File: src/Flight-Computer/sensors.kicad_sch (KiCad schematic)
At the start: 36 parts, among them P5 440054-3, P6 440054-3, P7 440054-3, P9 440054-3, Q3 QS5U17TR, Q4 QS5U17TR, Q5 QS5U17TR, Q6 QS5U17TR, U11 BMP390, U8 MPU-9250, U9 MAX-8C-0-10

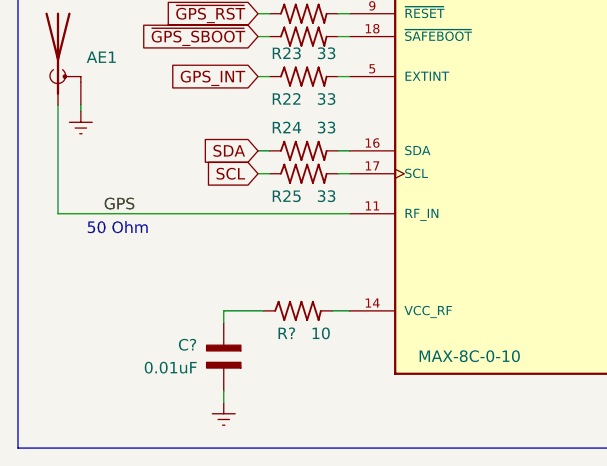
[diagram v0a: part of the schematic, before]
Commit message: added power supply for active gps antenna
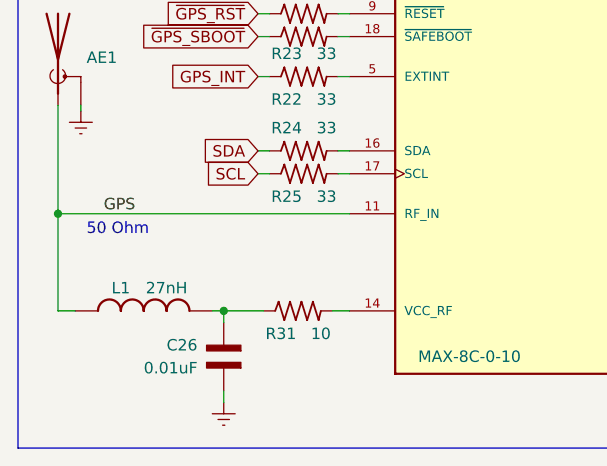
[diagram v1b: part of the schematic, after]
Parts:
- added L1: 27nH, symbol Flight-Computer:L-07C27NJV6T
- gave numbers to parts that had none: 2
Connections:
- net GPS: now also L1.1
- net at C26.1, R31.1: now also L1.2
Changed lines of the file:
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@@
   (junction (at 175.895 124.46) (diameter 0) (color 0 0 0 0)
   )
+  (junction (at 22.86 121.285) (diameter 0) (color 0 0 0 0)
+  )
   (junction (at 97.155 68.58) (diameter 0) (color 0 0 0 0)
   )
@@
   )
   (junction (at 97.155 38.1) (diameter 0) (color 0 0 0 0)
+  )
+  (junction (at 41.275 132.08) (diameter 0) (color 0 0 0 0)
   )
   (junction (at 232.41 40.005) (diameter 0) (color 0 0 0 0)
@@
     (stroke (width 0) (type default) (color 0 0 0 0))
   )
+  (wire (pts (xy 22.86 121.285) (xy 55.245 121.285))
+    (stroke (width 0) (type default) (color 0 0 0 0))
+  )
   (wire (pts (xy 100.965 123.825) (xy 102.235 123.825))
     (stroke (width 0) (type default) (color 0 0 0 0))
@@
     (stroke (width 0) (type default) (color 0 0 0 0))
   )
-  (wire (pts (xy 55.245 121.285) (xy 22.86 121.285))
-    (stroke (width 0) (type default) (color 0 0 0 0))
-  )
   (wire (pts (xy 97.155 53.34) (xy 97.155 38.1))
     (stroke (width 0) (type default) (color 0 0 0 0))
@@
     (stroke (width 0) (type default) (color 0 0 0 0))
   )
+  (wire (pts (xy 22.86 132.08) (xy 24.765 132.08))
+    (stroke (width 0) (type default) (color 0 0 0 0))
+  )
   (wire (pts (xy 232.41 95.885) (xy 232.41 105.41))
     (stroke (width 0) (type default) (color 0 0 0 0))
@@
     (stroke (width 0) (type default) (color 0 0 0 0))
   )
+  (wire (pts (xy 40.005 132.08) (xy 41.275 132.08))
+    (stroke (width 0) (type default) (color 0 0 0 0))
+  )
   (wire (pts (xy 121.285 35.56) (xy 121.285 36.83))
     (stroke (width 0) (type default) (color 0 0 0 0))
@@
   )
   (wire (pts (xy 53.34 132.08) (xy 55.245 132.08))
+    (stroke (width 0) (type default) (color 0 0 0 0))
+  )
+  (wire (pts (xy 22.86 121.285) (xy 22.86 132.08))
     (stroke (width 0) (type default) (color 0 0 0 0))
   )
@@
   (symbol (lib_id "Flight-Computer:Earth") (at 41.275 142.24 0) (unit 1)
     (in_bom yes) (on_board yes) (fields_autoplaced)
-    (property "Reference" "#PWR?" (id 0) (at 41.275 148.59 0)
+    (property "Reference" "#PWR057" (id 0) (at 41.275 148.59 0)
       (effects (font (size 1.27 1.27)) hide)
     )
@@
   (symbol (lib_id "Flight-Computer:RES_0603") (at 49.53 132.08 0) (unit 1)
     (in_bom yes) (on_board yes)
-    (property "Reference" "R?" (id 0) (at 48.26 134.62 0))
+    (property "Reference" "R31" (id 0) (at 47.625 134.62 0))
     (property "Value" "10" (id 1) (at 52.07 134.62 0))
     (property "Footprint" "" (id 2) (at 50.8 144.78 0)
@@
     )
     (pin "1")
+  )
+  (symbol (lib_id "Flight-Computer:L-07C27NJV6T") (at 32.385 132.08 0) (unit 1)
+    (in_bom yes) (on_board yes)
+    (property "Reference" "L1" (id 0) (at 29.845 129.54 0))
+    (property "Value" "27nH" (id 1) (at 34.925 129.54 0))
+    (property "Footprint" "" (id 2) (at 28.575 137.16 0)
+      (effects (font (size 1.27 1.27)) (justify left bottom) hide)
+    )
+    (property "Datasheet" "" (id 3) (at 32.385 132.08 0)
+      (effects (font (size 1.27 1.27)) (justify left bottom) hide)
+    )
+    (pin "1")
+    (pin "2")
   )
   (symbol (lib_id "Flight-Computer:RES_0603") (at 50.165 114.3 0) (unit 1)
@@
   (symbol (lib_id "Flight-Computer:CAP_0603") (at 41.275 137.16 90) (unit 1)
     (in_bom yes) (on_board yes)
-    (property "Reference" "C?" (id 0) (at 36.195 135.89 90)
+    (property "Reference" "C26" (id 0) (at 34.925 135.89 90)
       (effects (font (size 1.27 1.27)) (justify right))
     )

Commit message: plotted schematic to pdf
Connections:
- no-connect marks 7 -> 6
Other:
- note removed: "TODO: Add antenna power connections"
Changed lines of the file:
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@@
   (junction (at 52.705 55.88) (diameter 0) (color 0 0 0 0)
   )
-  (no_connect (at 100.965 106.045))
   (no_connect (at 100.965 127.635))
   (no_connect (at 100.965 111.125))
@@
     (stroke (width 0) (type default) (color 0 0 0 0))
   )
-  (text "TODO: Add antenna\npower connections" (at 103.505 109.855 0)
-    (effects (font (size 1.27 1.27)) (justify left bottom))
-  )
   (text "Servo Motor PWM Interface" (at 187.325 86.995 0)

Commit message: added mcu signals for peripherals
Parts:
- AE1: footprint (none) -> Flight-Computer:73412-0110
- BT1: footprint (none) -> Flight-Computer:MS621FE-FL11E
- C20, C21, C22, C24, C25, C26: footprint (none) -> Flight-Computer:CAP_0603
- D10, D7, D8, D9: footprint (none) -> Flight-Computer:MM3Z3V3B
- L1: footprint (none) -> Flight-Computer:L-07C27NJV6T
- P5, P6, P7, P9: footprint CONN_4840.2201_SCH -> Flight-Computer:440054-3
- R19, R20, R21, R22, R23, R24, R25, R26, R27, R28, R29, R30, R31: footprint (none) -> Flight-Computer:RES_0603
- U11: footprint XDCR_BMP390L -> Flight-Computer:BMP390
- U8: footprint QFN40P300X300X105-24N -> Flight-Computer:MPU-9250
- U9: footprint XCVR_MAX-8C-0-10 -> Flight-Computer:MAX-8C-0

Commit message: setup layout design rules
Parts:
- Q3, Q4, Q5, Q6: footprint Package_TO_SOT_THT:TO-92_Inline -> Engine-Controller:QS5U17TR
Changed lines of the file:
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@@
     (pin "1")
   )
-  (symbol (lib_id "Flight-Computer:QS5U17TR") (at 182.88 104.775 0) (unit 1)
+  (symbol (lib_name "QS5U17TR_1") (lib_id "Flight-Computer:QS5U17TR") (at 182.88 104.775 0) (unit 1)
     (in_bom yes) (on_board yes) (fields_autoplaced)
     (property "Reference" "Q3" (id 0) (at 188.087 105.2088 0)
@@
       (effects (font (size 1.27 1.27)) (justify left) hide)
     )
-    (property "Footprint" "Package_TO_SOT_THT:TO-92_Inline" (id 2) (at 184.785 120.65 0)
+    (property "Footprint" "Engine-Controller:QS5U17TR" (id 2) (at 184.785 120.65 0)
       (effects (font (size 1.27 1.27) italic) (justify left) hide)
     )
@@
     (pin "1")
     (pin "2")
+    (pin "3")
+    (pin "4")
     (pin "5")
   )
@@
     (pin "2")
   )
-  (symbol (lib_id "Flight-Computer:QS5U17TR") (at 182.88 132.715 0) (unit 1)
+  (symbol (lib_name "QS5U17TR_2") (lib_id "Flight-Computer:QS5U17TR") (at 182.88 132.715 0) (unit 1)
     (in_bom yes) (on_board yes) (fields_autoplaced)
     (property "Reference" "Q4" (id 0) (at 188.087 133.1488 0)
@@
       (effects (font (size 1.27 1.27)) (justify left) hide)
     )
-    (property "Footprint" "Package_TO_SOT_THT:TO-92_Inline" (id 2) (at 184.785 148.59 0)
+    (property "Footprint" "Engine-Controller:QS5U17TR" (id 2) (at 184.785 148.59 0)
       (effects (font (size 1.27 1.27) italic) (justify left) hide)
     )
@@
     (pin "1")
     (pin "2")
+    (pin "3")
+    (pin "4")
     (pin "5")
   )
@@
       (effects (font (size 1.27 1.27)) (justify left) hide)
     )
-    (property "Footprint" "Package_TO_SOT_THT:TO-92_Inline" (id 2) (at 241.3 120.015 0)
+    (property "Footprint" "Engine-Controller:QS5U17TR" (id 2) (at 241.3 120.015 0)
       (effects (font (size 1.27 1.27) italic) (justify left) hide)
     )
@@
     (pin "1")
     (pin "2")
+    (pin "3")
+    (pin "4")
     (pin "5")
   )
@@
     (pin "1")
   )
-  (symbol (lib_id "Flight-Computer:QS5U17TR") (at 239.395 132.08 0) (unit 1)
+  (symbol (lib_name "QS5U17TR_3") (lib_id "Flight-Computer:QS5U17TR") (at 239.395 132.08 0) (unit 1)
     (in_bom yes) (on_board yes) (fields_autoplaced)
     (property "Reference" "Q6" (id 0) (at 244.602 132.5138 0)
@@
       (effects (font (size 1.27 1.27)) (justify left) hide)
     )
-    (property "Footprint" "Package_TO_SOT_THT:TO-92_Inline" (id 2) (at 241.3 147.955 0)
+    (property "Footprint" "Engine-Controller:QS5U17TR" (id 2) (at 241.3 147.955 0)
       (effects (font (size 1.27 1.27) italic) (justify left) hide)
     )
@@
     (pin "1")
     (pin "2")
+    (pin "3")
+    (pin "4")
     (pin "5")
   )
@@
     (pin "8")
     (pin "9")
+    (pin "14")
+    (pin "15")
+    (pin "16")
+    (pin "17")
+    (pin "2")
+    (pin "3")
+    (pin "4")
+    (pin "5")
+    (pin "6")
   )
   (symbol (lib_id "Flight-Computer:MS614SE-FL28E") (at 125.73 107.315 0) (unit 1)

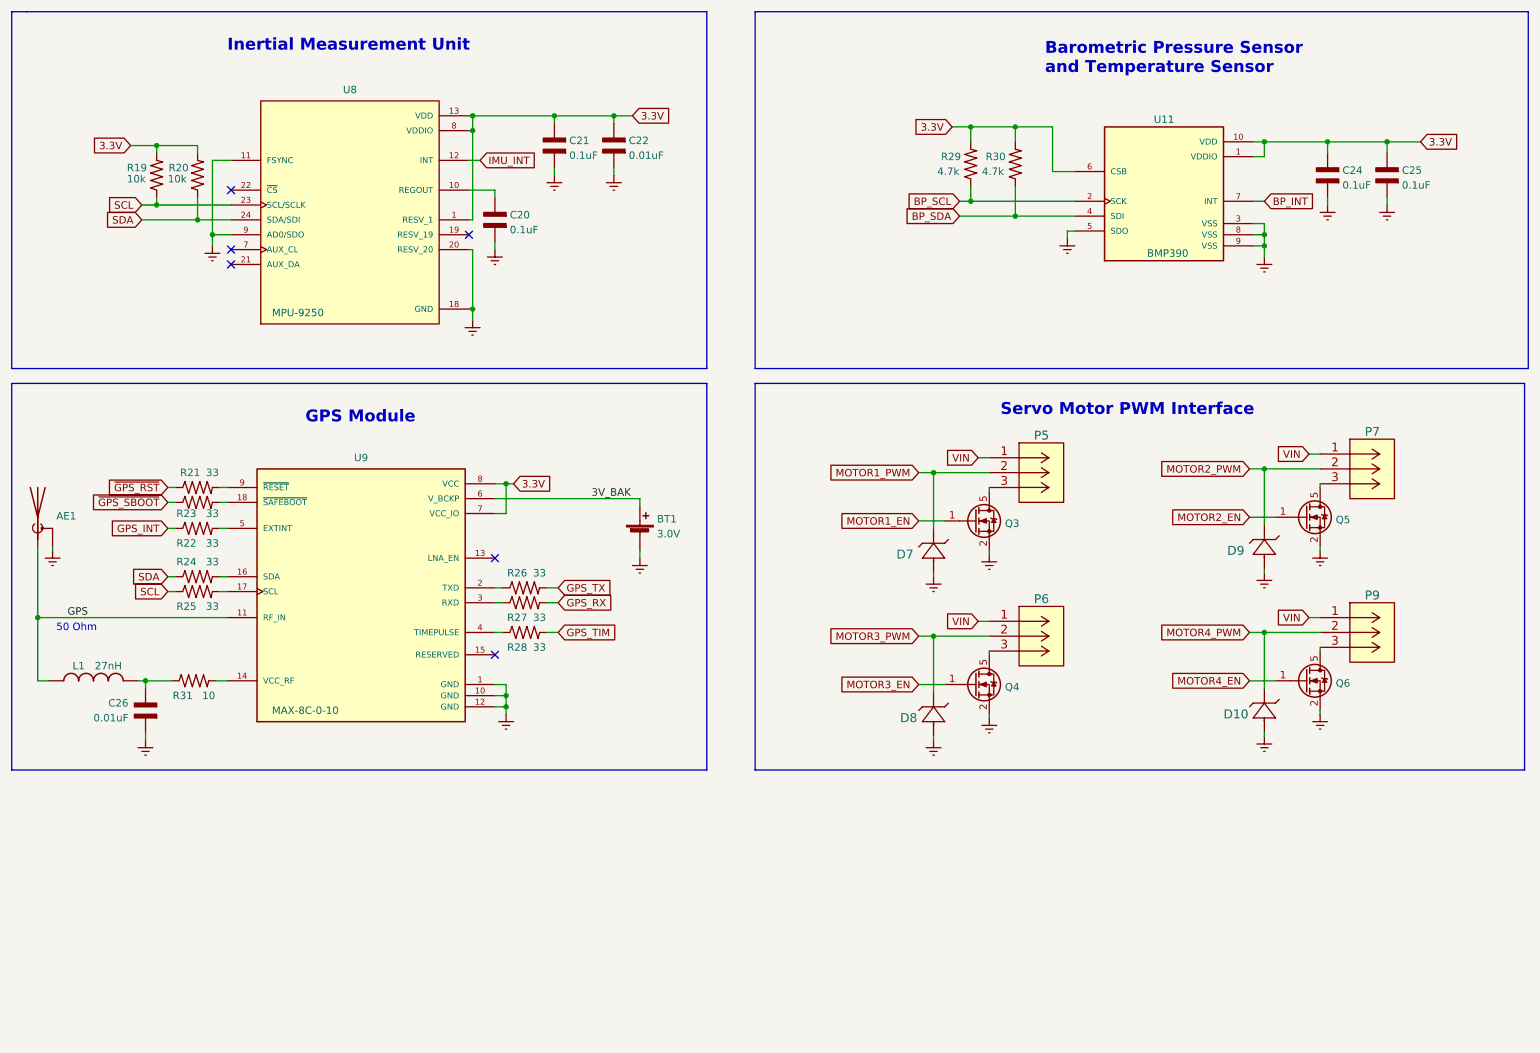
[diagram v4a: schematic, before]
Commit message: added usb detector to schemtaic
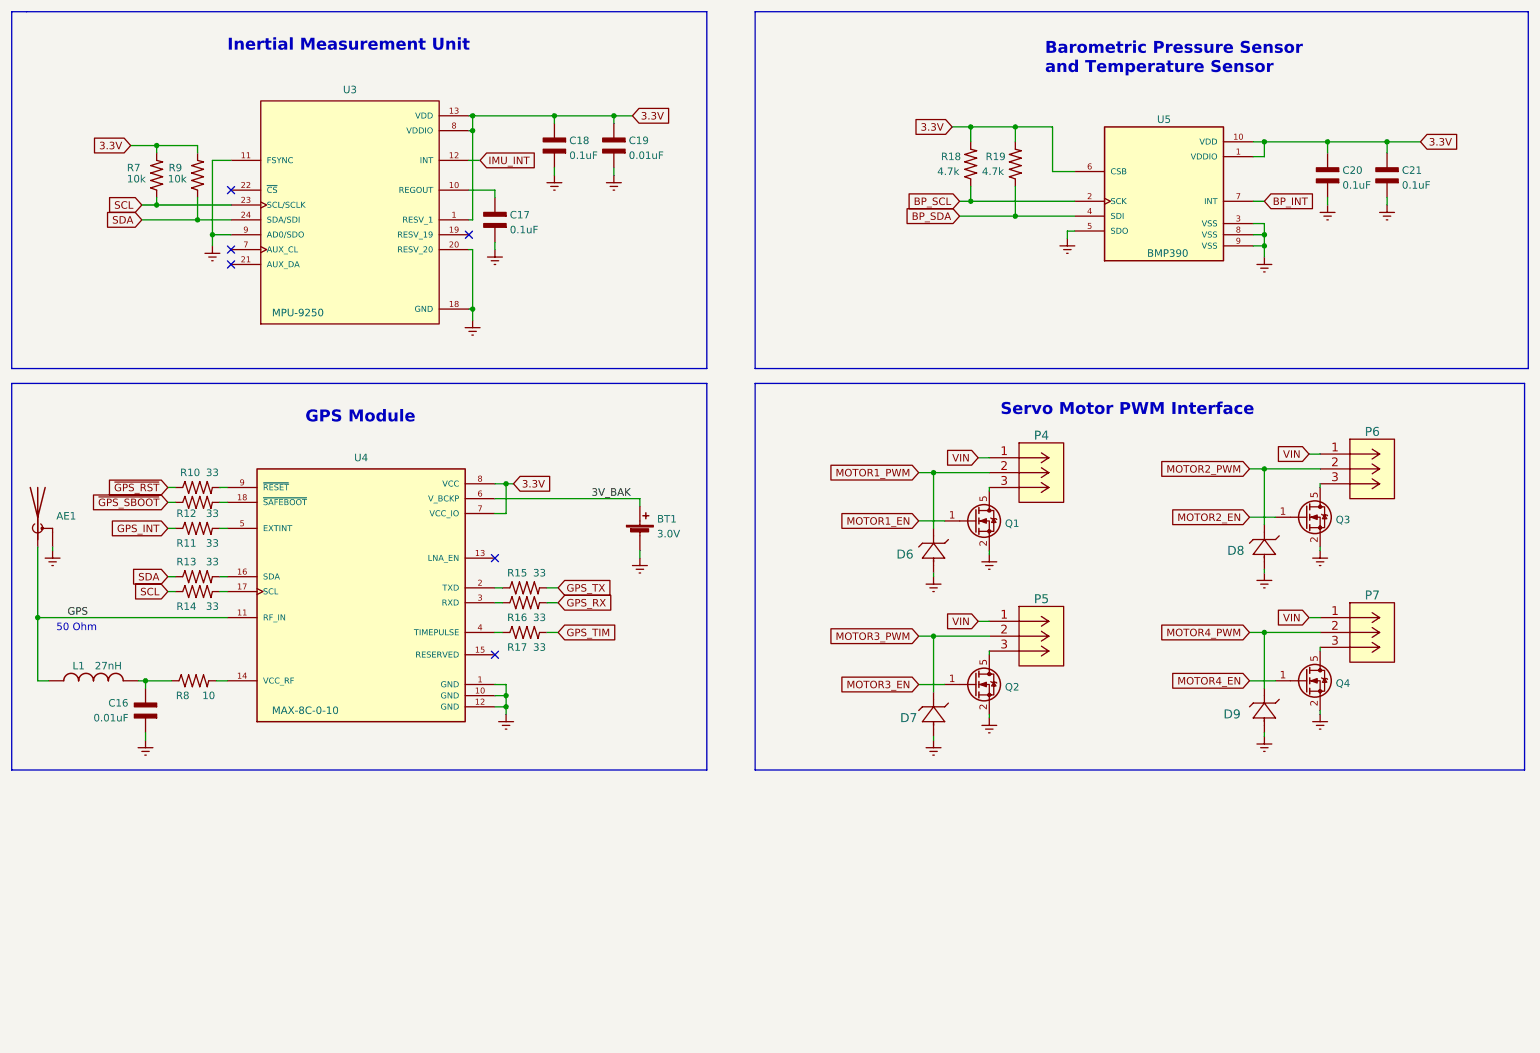
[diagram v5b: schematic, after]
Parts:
- renumbered C26 to C16, C20 to C17, C21 to C18, C22 to C19, C24 to C20, C25 to C21, D7 to D6, D8 to D7, D9 to D8, D10 to D9, P5 to P4, P6 to P5, P7 to P6, P9 to P7, Q3 to Q1, Q4 to Q2, Q5 to Q3, Q6 to Q4, R21 to R10, R22 to R11, R23 to R12, R24 to R13, R25 to R14, R26 to R15, R27 to R16, R28 to R17, R29 to R18, R30 to R19, R19 to R7, R31 to R8, R20 to R9, U8 to U3, U9 to U4, U11 to U5

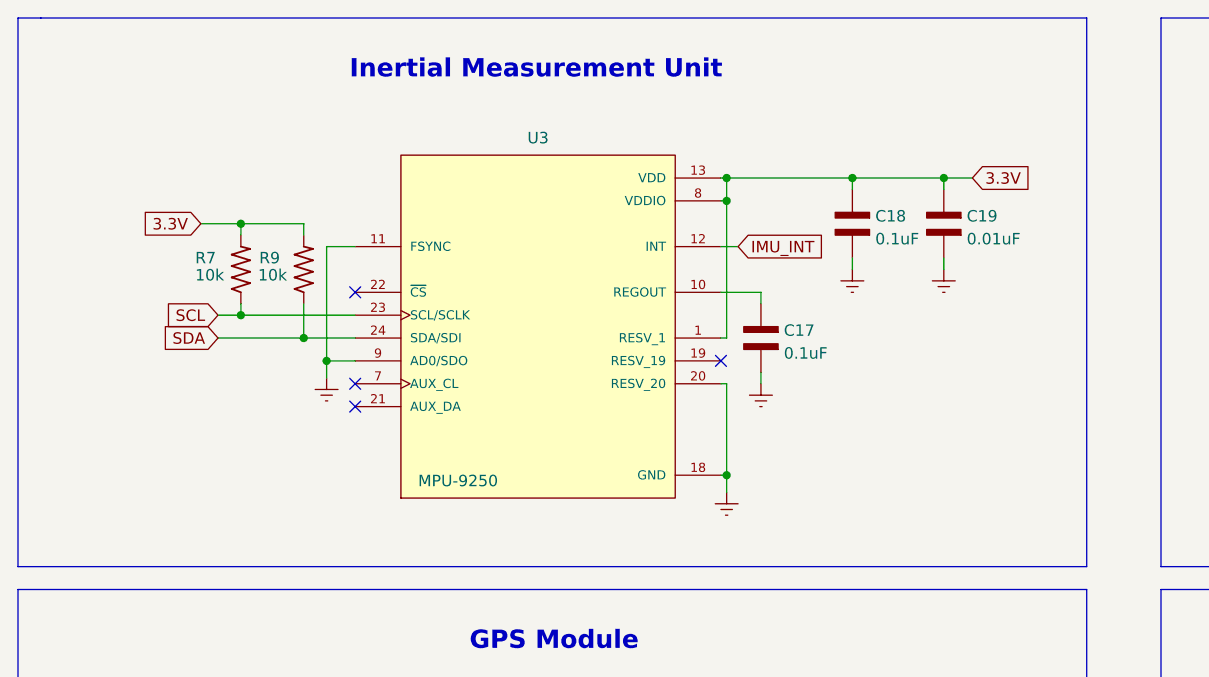
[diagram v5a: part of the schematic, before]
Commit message: implemented new imu in schematic
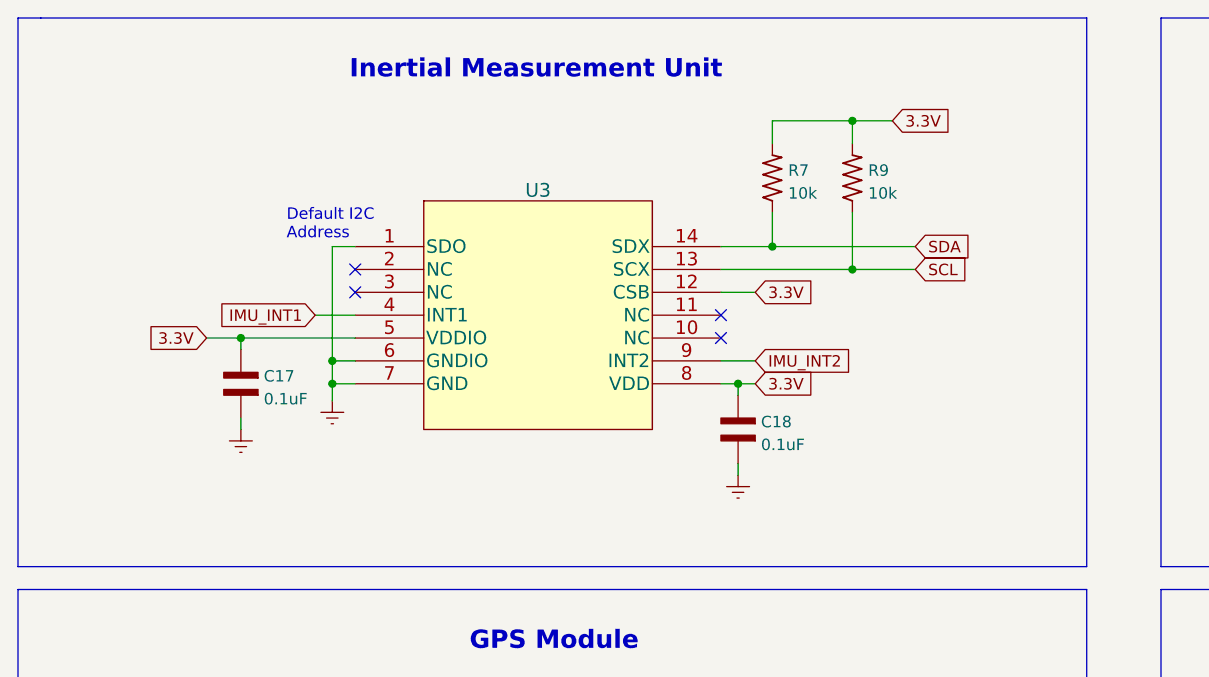
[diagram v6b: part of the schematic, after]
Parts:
- removed C19: 0.01uF, Flight-Computer:CAP_0603, symbol Flight-Computer:CAP_0603
- removed U3: MPU-9250, Flight-Computer:MPU-9250, symbol Flight-Computer:MPU-9250
- added U3: BMI323, Flight-Computer:BMI323, symbol Flight-Computer:BMI323
- R7, R9: footprint Flight-Computer:RES_0603 -> (none)
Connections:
- net 3.3V: now also C17.1, U3.12 (CSB), U3.5 (VDDIO), U3.8 (VDD)
- net Earth: now also U3.1 (SDO), U3.6 (GNDIO), U3.7 (GND)
- net SCL: now also R9.1, U3.13 (SCX); no longer R7.1
- net SDA: now also R7.1, U3.14 (SDX); no longer R9.1
- new net IMU_INT1: U3.4 (INT1)
- new net IMU_INT2: U3.9 (INT2)
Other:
- note added: "Default I2C Address"
